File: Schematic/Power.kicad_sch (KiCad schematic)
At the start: 37 parts, among them IC1 MP9943AGQ-Z, IC2 MP9943AGQ-Z, U2 ME6217C33M5G

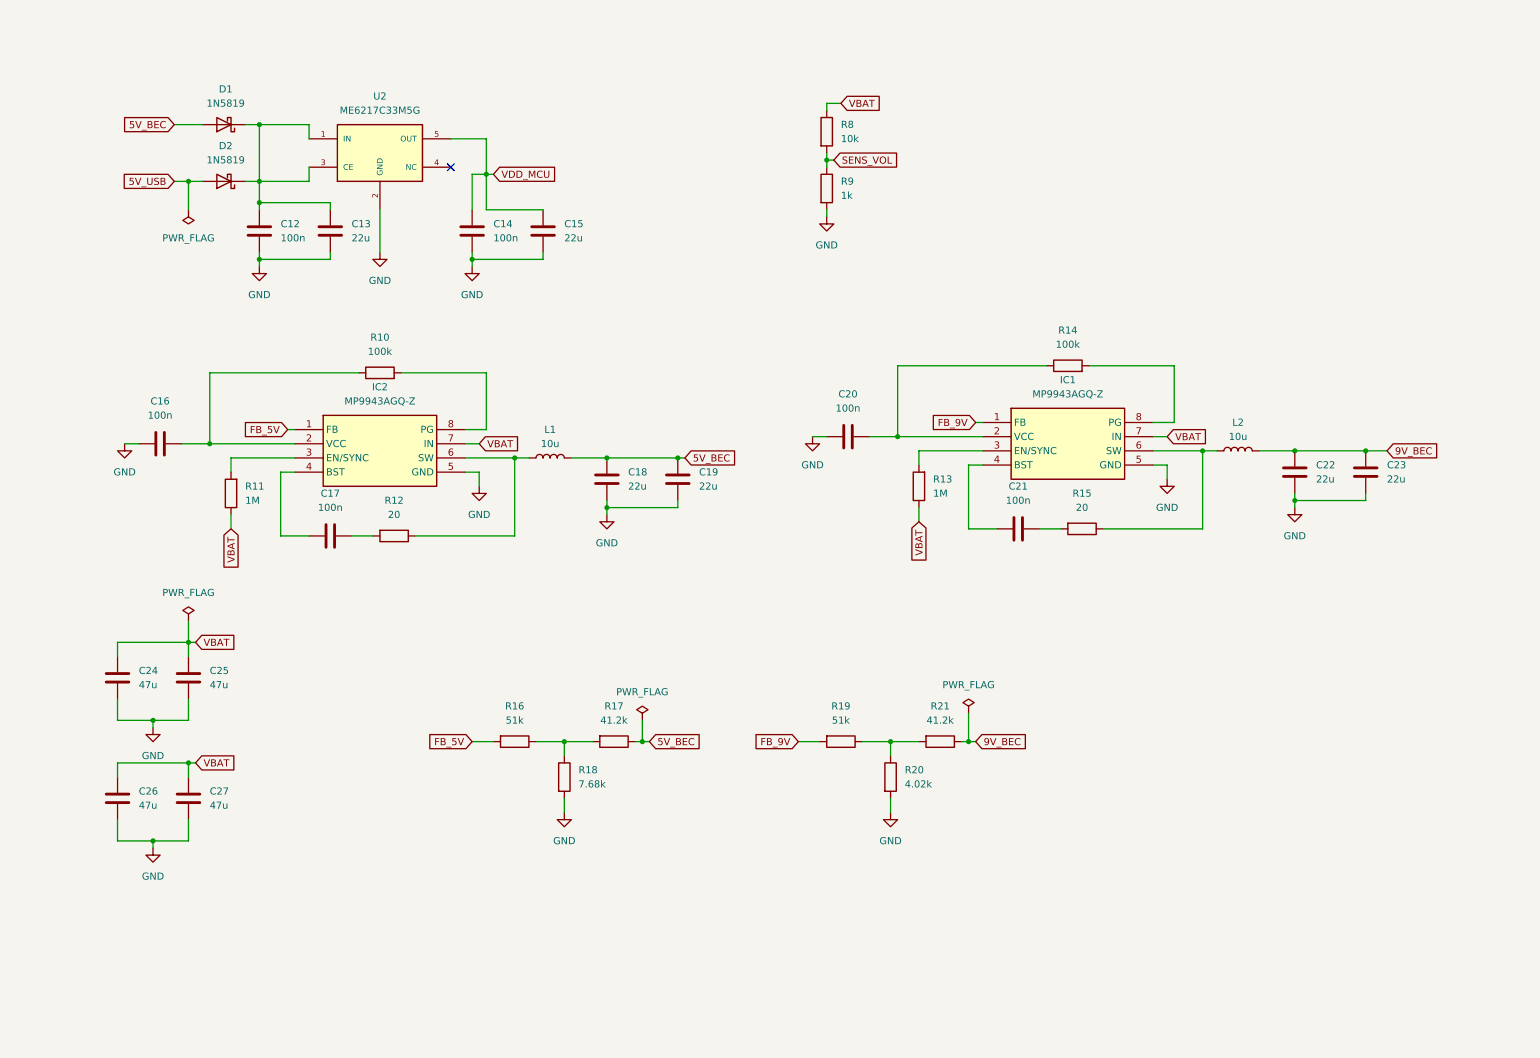
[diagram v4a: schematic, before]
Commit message: Refactor schematic files and update component placements
- Adjusted component positions in osd.kicad_sch for better layout.
- Added new junctions and wires in rf_rx.kicad_sch to improve connectivity.
- Introduced additional junctions and wires in sensors.kicad_sch for enhanced signal routing.
- Removed outdated backup file fch7-2025-11-18_191836.zip and added new backup fch7-2025-11-27_202230.zip.
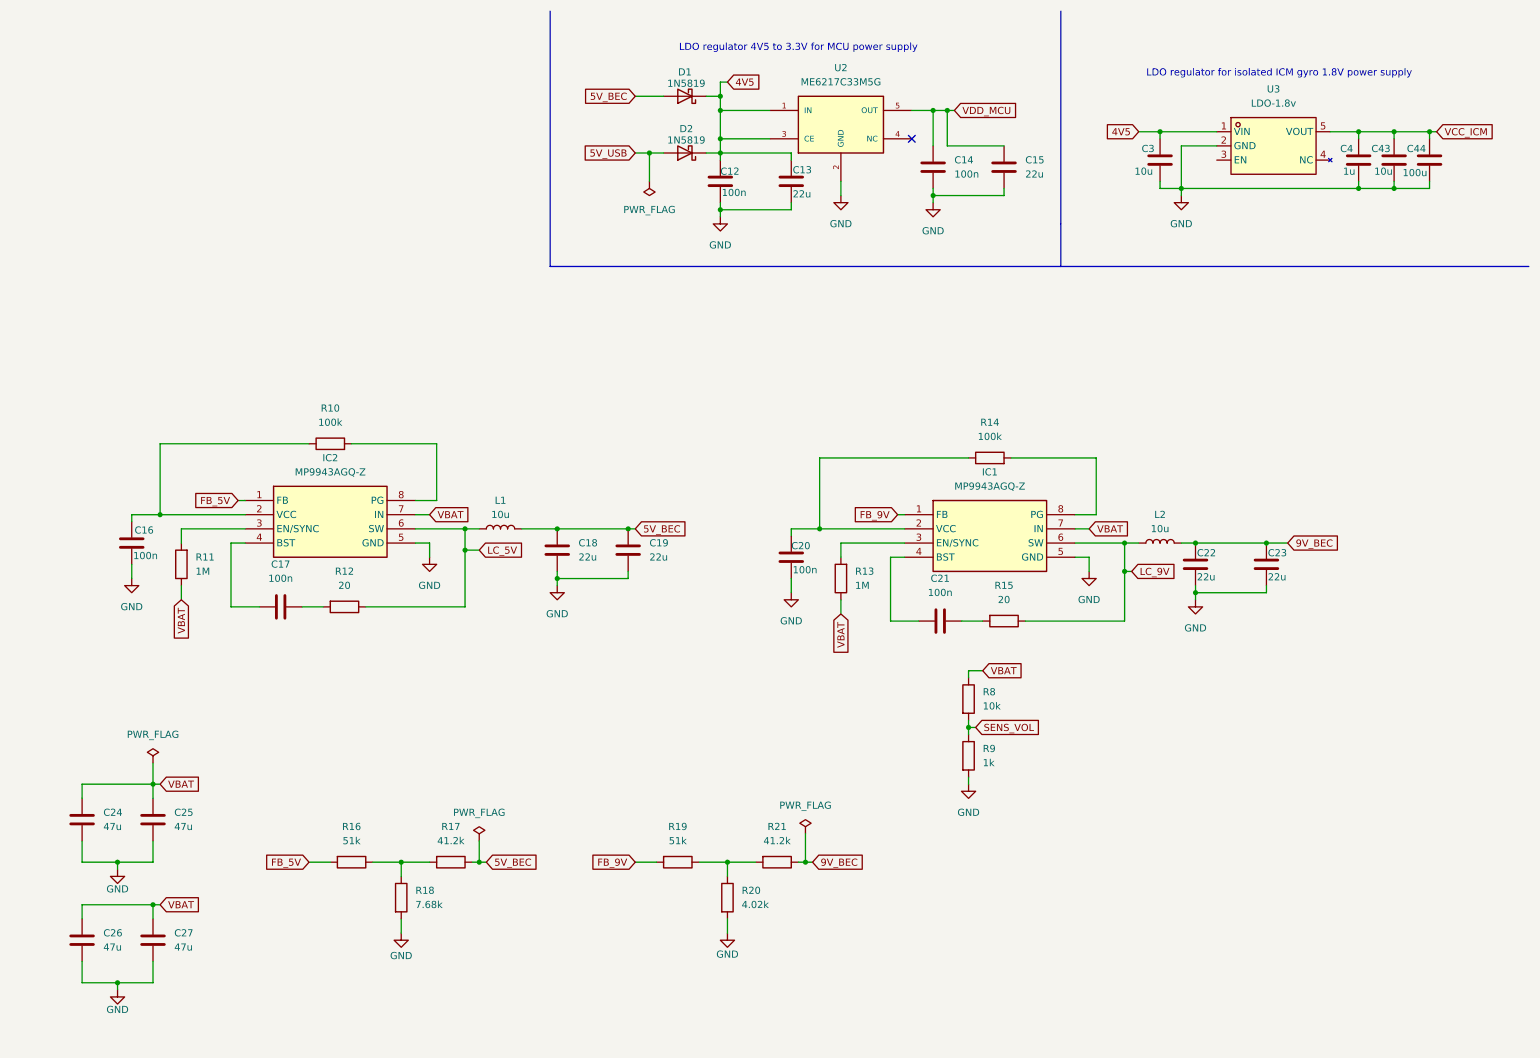
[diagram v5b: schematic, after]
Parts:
- added C3, C43: 10u, Capacitor_SMD:C_0805_2012Metric, symbol Device:C
- added C4: 1u, Capacitor_SMD:C_0805_2012Metric, symbol Device:C
- added C44: 100u, Capacitor_SMD:C_0805_2012Metric, symbol Device:C
- added U3: LDO-1.8v, fch7_fp:AP2112K-1.8TRG1, symbol fch7_sym:AP2112K-1.8TRG1
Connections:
- net GND: now also C3.2, C4.2, C43.2, C44.2, U3.2 (GND)
- net LC_5V: now reaches IC2.6 (SW), L1.1, R12.1
- net LC_9V: now reaches IC1.6 (SW), L2.1, R15.1
- net 4V5: now reaches C12.1, C13.1, D1.1 (K), D2.1 (K), U2.1 (IN), U2.3 (CE)
- net 4V5: now also C3.1, U3.1 (VIN)
- new net VCC_ICM: C4.1, C43.1, C44.1, U3.5 (VOUT)
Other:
- note added: "LDO regulator 4V5 to 3.3V for MCU power supply"
- note added: "LDO regulator for isolated ICM gyro 1.8V power supply"
- moved on the sheet: C12, C13, C14, C15, C16, C17, C18, C19, C20, C21, C22, C23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

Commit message: Refactor code structure for improved readability and maintainability
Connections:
- no-connect marks 1 -> 2
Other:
- note added: "VBAT filtering, absorbing and smoothing input voltage from motor pulling"
- note added: "Voltage divider bridge for buck regulator feedback"
- note added: "voltage divider bridge for battery voltage sensor on PC0 MCU pin (ratio = 11 for 6S voltage 25.2/11=2.29)"
- moved on the sheet: C24, C25, C26, C27, R16, R17, R18, R19, R20, R21, R8, R9

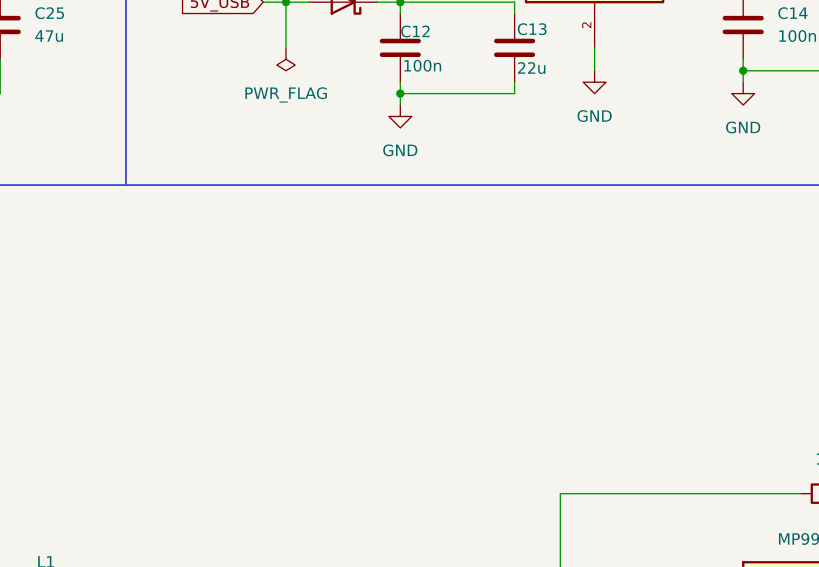
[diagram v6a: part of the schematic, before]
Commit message: refactor : improve readability and portability of the project
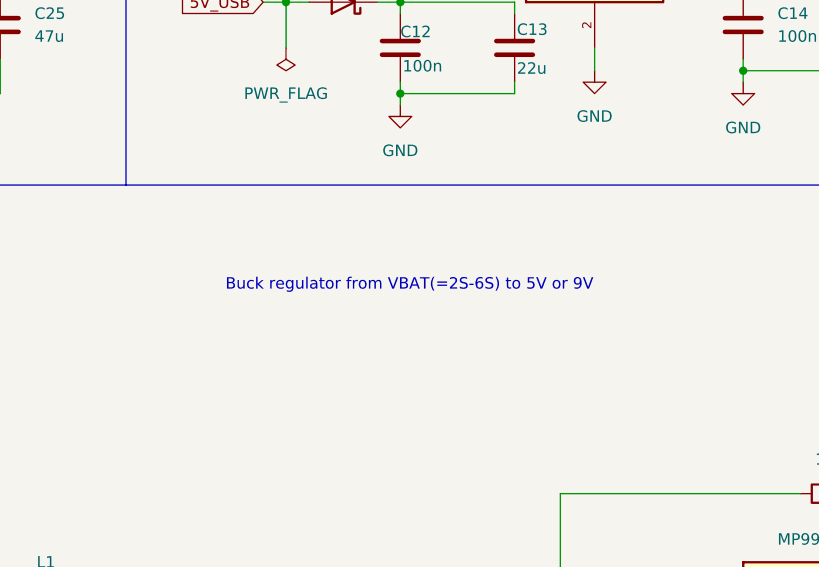
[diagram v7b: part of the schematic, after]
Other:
- note added: "Buck regulator from VBAT(=2S-6S) to 5V or 9V"
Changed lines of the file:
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@@
+		)
+	)
+	(text "Buck regulator from VBAT(=2S-6S) to 5V or 9V\n "
+		(exclude_from_sim no)
+		(at 140.716 70.612 0)
+		(effects
+			(font
+				(size 1.27 1.27)
+			)
 		)
 	)
